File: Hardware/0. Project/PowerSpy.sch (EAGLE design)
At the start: 91 parts, among them IC1 CP2102N-A01-GQFN28, IC3 LM324D, P1 Mini-Fit 4T, T1 SS8050, T2 SS8050, U1 NCP1117ST33T3G, U2 HLK-PM01, U3 ADS1115IDGST, U4 ESP32-WROOM-32D, X1 4T PJ-321, X2 4T PJ-321, X3 USB Micro B

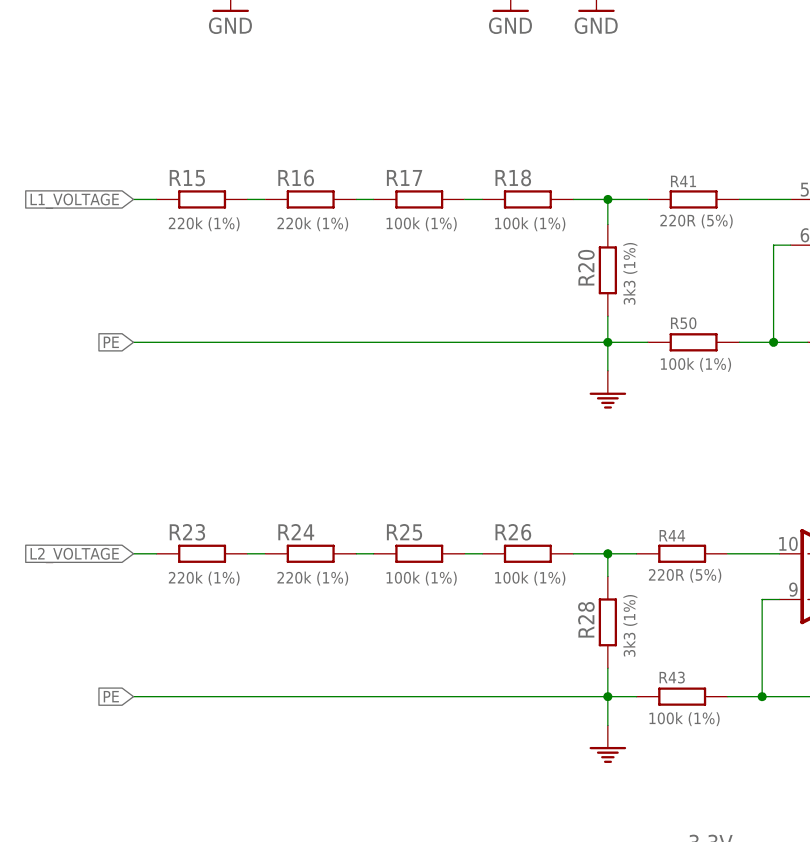
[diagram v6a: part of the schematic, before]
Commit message: Calcs and values updated for the new AFE approach
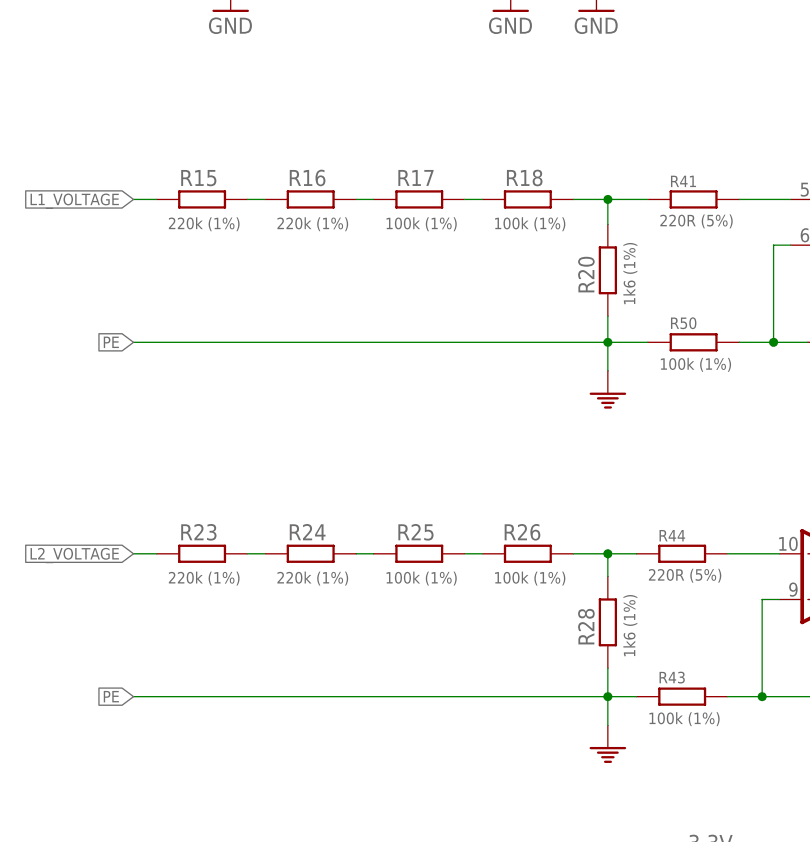
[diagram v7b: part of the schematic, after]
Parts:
- R20, R28: value 3k3 (1%) -> 1k6 (1%)
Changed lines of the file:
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@@
 <setting verticaltext="up"/>
 </settings>
-<grid distance="0.025" unitdist="inch" unit="inch" style="lines" multiple="1" display="no" altdistance="0.01" altunitdist="inch" altunit="inch"/>
+<grid distance="0.1" unitdist="inch" unit="inch" style="lines" multiple="1" display="no" altdistance="0.01" altunitdist="inch" altunit="inch"/>
 <layers>
 <layer number="1" name="Top" color="4" fill="1" visible="no" active="no"/>
@@
 <part name="R16" library="rcl" library_urn="urn:adsk.eagle:library:334" deviceset="R-EU_" device="R0603" package3d_urn="urn:adsk.eagle:package:23555/3" value="220k (1%)"/>
 <part name="R15" library="rcl" library_urn="urn:adsk.eagle:library:334" deviceset="R-EU_" device="R0603" package3d_urn="urn:adsk.eagle:package:23555/3" value="220k (1%)"/>
-<part name="R20" library="rcl" library_urn="urn:adsk.eagle:library:334" deviceset="R-EU_" device="R0603" package3d_urn="urn:adsk.eagle:package:23555/3" value="3k3 (1%)"/>
+<part name="R20" library="rcl" library_urn="urn:adsk.eagle:library:334" deviceset="R-EU_" device="R0603" package3d_urn="urn:adsk.eagle:package:23555/3" value="1k6 (1%)"/>
 <part name="R19" library="rcl" library_urn="urn:adsk.eagle:library:334" deviceset="R-EU_" device="R0603" package3d_urn="urn:adsk.eagle:package:23555/3" value="47R (5%)"/>
 <part name="C7" library="rcl" library_urn="urn:adsk.eagle:library:334" deviceset="C-EU" device="C0603K" package3d_urn="urn:adsk.eagle:package:23680/2" value="10nF/50V (10%)"/>
@@
 <part name="R24" library="rcl" library_urn="urn:adsk.eagle:library:334" deviceset="R-EU_" device="R0603" package3d_urn="urn:adsk.eagle:package:23555/3" value="220k (1%)"/>
 <part name="R23" library="rcl" library_urn="urn:adsk.eagle:library:334" deviceset="R-EU_" device="R0603" package3d_urn="urn:adsk.eagle:package:23555/3" value="220k (1%)"/>
-<part name="R28" library="rcl" library_urn="urn:adsk.eagle:library:334" deviceset="R-EU_" device="R0603" package3d_urn="urn:adsk.eagle:package:23555/3" value="3k3 (1%)"/>
+<part name="R28" library="rcl" library_urn="urn:adsk.eagle:library:334" deviceset="R-EU_" device="R0603" package3d_urn="urn:adsk.eagle:package:23555/3" value="1k6 (1%)"/>
 <part name="R39" library="rcl" library_urn="urn:adsk.eagle:library:334" deviceset="R-EU_" device="R0603" package3d_urn="urn:adsk.eagle:package:23555/3" value="1M (5%)"/>
 <part name="GND32" library="supply1" library_urn="urn:adsk.eagle:library:371" deviceset="GND" device=""/>
@@
 </instance>
 <instance part="R18" gate="G$1" x="76.2" y="132.08" smashed="yes">
-<attribute name="NAME" x="72.39" y="133.5786" size="1.778" layer="95"/>
+<attribute name="NAME" x="73.66" y="133.5786" size="1.778" layer="95"/>
 <attribute name="VALUE" x="72.39" y="128.778" size="1.27" layer="96"/>
 </instance>
 <instance part="R17" gate="G$1" x="64.135" y="132.08" smashed="yes">
-<attribute name="NAME" x="60.325" y="133.5786" size="1.778" layer="95"/>
+<attribute name="NAME" x="61.595" y="133.5786" size="1.778" layer="95"/>
 <attribute name="VALUE" x="60.325" y="128.778" size="1.27" layer="96"/>
 </instance>
 <instance part="R16" gate="G$1" x="52.07" y="132.08" smashed="yes">
-<attribute name="NAME" x="48.26" y="133.5786" size="1.778" layer="95"/>
+<attribute name="NAME" x="49.53" y="133.5786" size="1.778" layer="95"/>
 <attribute name="VALUE" x="48.26" y="128.778" size="1.27" layer="96"/>
 </instance>
 <instance part="R15" gate="G$1" x="40.005" y="132.08" smashed="yes">
-<attribute name="NAME" x="36.195" y="133.5786" size="1.778" layer="95"/>
+<attribute name="NAME" x="37.465" y="133.5786" size="1.778" layer="95"/>
 <attribute name="VALUE" x="36.195" y="128.778" size="1.27" layer="96"/>
 </instance>
 <instance part="R20" gate="G$1" x="85.09" y="124.206" smashed="yes" rot="R270">
-<attribute name="NAME" x="83.5914" y="122.301" size="1.778" layer="95" rot="R90"/>
+<attribute name="NAME" x="83.5914" y="121.539" size="1.778" layer="95" rot="R90"/>
 <attribute name="VALUE" x="86.868" y="127.381" size="1.27" layer="96" rot="R270"/>
 </instance>
@@
 </instance>
 <instance part="R26" gate="G$1" x="76.2" y="92.71" smashed="yes">
-<attribute name="NAME" x="72.39" y="94.2086" size="1.778" layer="95"/>
+<attribute name="NAME" x="73.406" y="94.2086" size="1.778" layer="95"/>
 <attribute name="VALUE" x="72.39" y="89.408" size="1.27" layer="96"/>
 </instance>
 <instance part="R25" gate="G$1" x="64.135" y="92.71" smashed="yes">
-<attribute name="NAME" x="60.325" y="94.2086" size="1.778" layer="95"/>
+<attribute name="NAME" x="61.595" y="94.2086" size="1.778" layer="95"/>
 <attribute name="VALUE" x="60.325" y="89.408" size="1.27" layer="96"/>
 </instance>
 <instance part="R24" gate="G$1" x="52.07" y="92.71" smashed="yes">
-<attribute name="NAME" x="48.26" y="94.2086" size="1.778" layer="95"/>
+<attribute name="NAME" x="49.53" y="94.2086" size="1.778" layer="95"/>
 <attribute name="VALUE" x="48.26" y="89.408" size="1.27" layer="96"/>
 </instance>
 <instance part="R23" gate="G$1" x="40.005" y="92.71" smashed="yes">
-<attribute name="NAME" x="36.195" y="94.2086" size="1.778" layer="95"/>
+<attribute name="NAME" x="37.465" y="94.2086" size="1.778" layer="95"/>
 <attribute name="VALUE" x="36.195" y="89.408" size="1.27" layer="96"/>
 </instance>
 <instance part="R28" gate="G$1" x="85.09" y="85.09" smashed="yes" rot="R270">
-<attribute name="NAME" x="83.5914" y="83.185" size="1.778" layer="95" rot="R90"/>
+<attribute name="NAME" x="83.5914" y="82.423" size="1.778" layer="95" rot="R90"/>
 <attribute name="VALUE" x="86.868" y="88.265" size="1.27" layer="96" rot="R270"/>
 </instance>

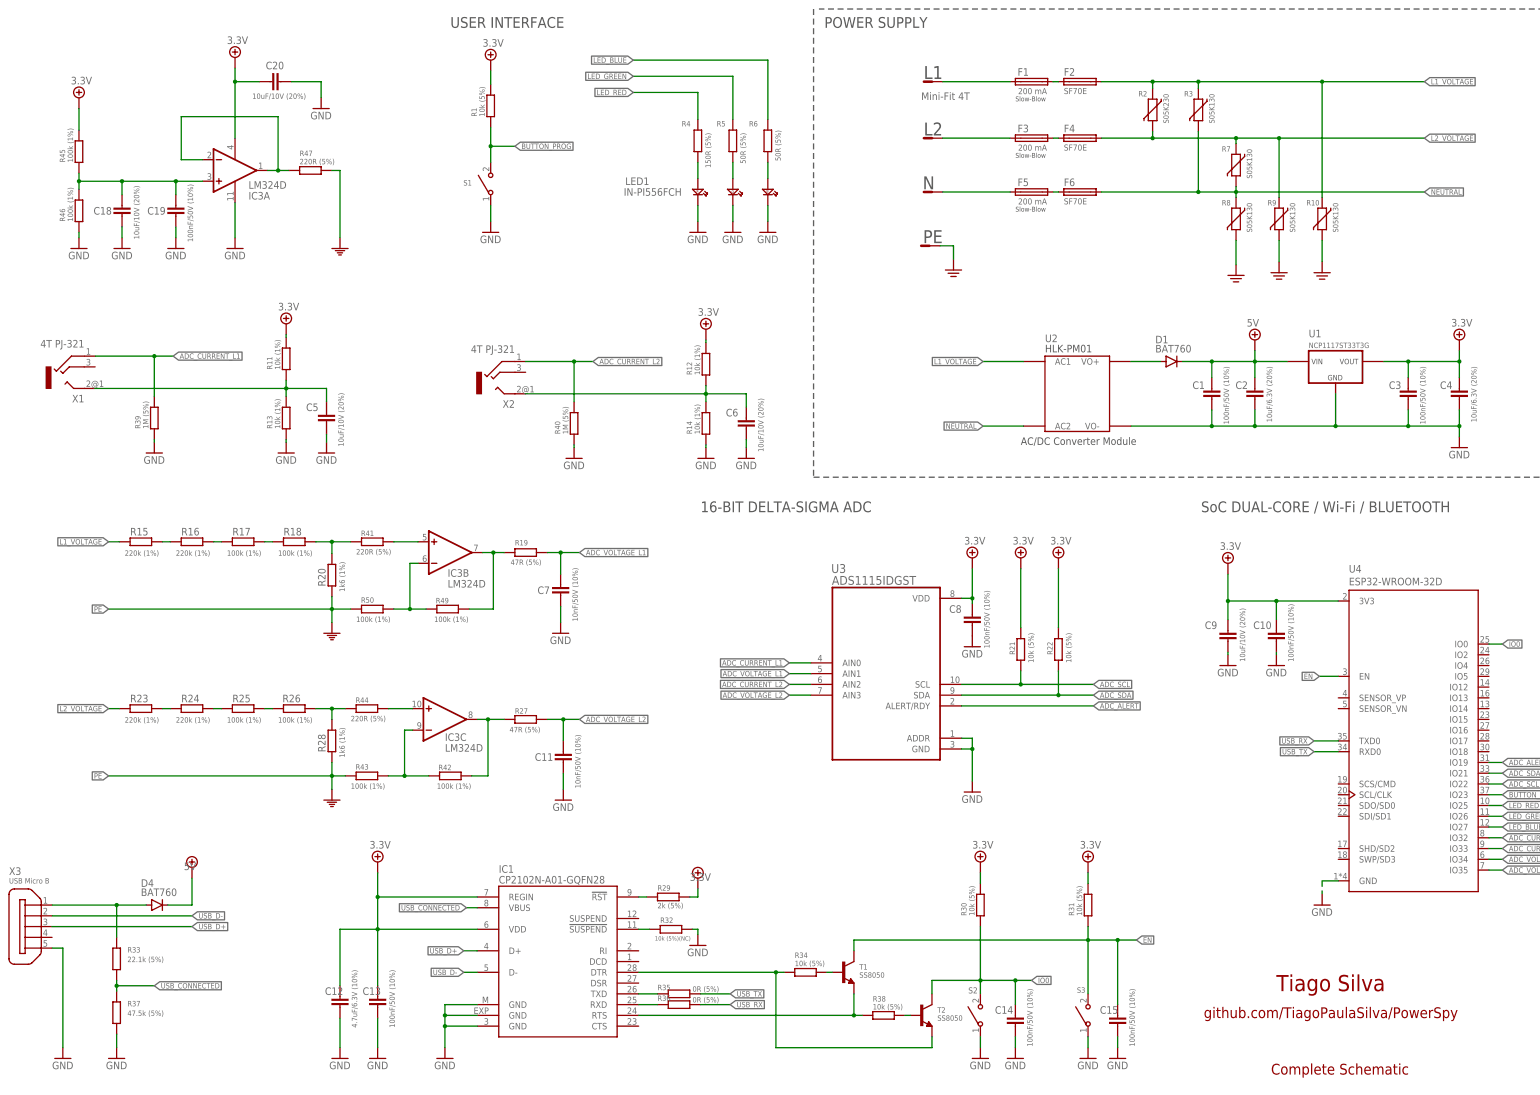
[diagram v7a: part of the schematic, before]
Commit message: Schematic parts renumbered
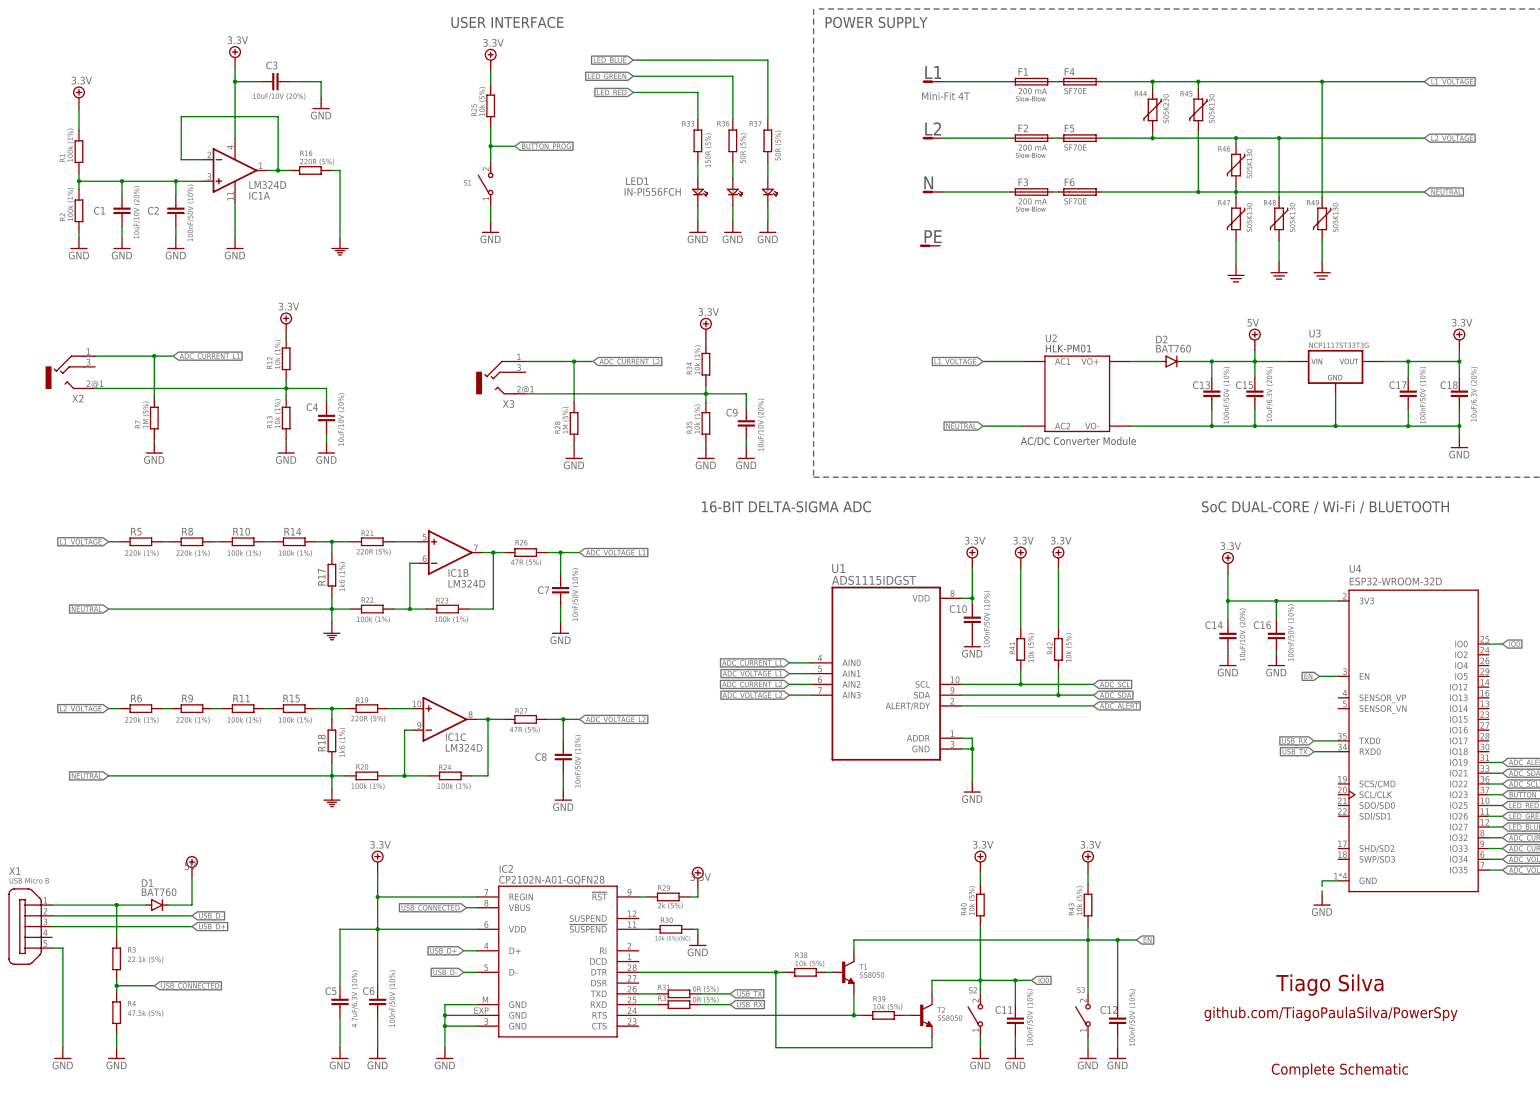
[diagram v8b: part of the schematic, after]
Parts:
- removed C19: 100nF/50V (10%), rcl:C-EUC0603K
- removed C20: 10uF/10V (20%), rcl:C-EUC0603K
- removed D4: BAT760, diode:DIODE-SOD323-W
- removed IC3: LM324D, linear:LM324D
- removed R50: 100k (1%), rcl:R-EU_R0603
- added C16, C17: 100nF/50V (10%), rcl:C-EUC0603K
- added D2: BAT760, diode:DIODE-SOD323-W
- added IC2: CP2102N-A01-GQFN28, silabs:CP2102
- added R48: S05K130, varistor:VARISTORS05K11
- C1, C14, C3: value 100nF/50V (10%) -> 10uF/10V (20%)
- C11: value 10nF/50V (10%) -> 100nF/50V (10%)
- C12: value 4.7uF/6.3V (10%) -> 100nF/50V (10%)
- C15: value 100nF/50V (10%) -> 10uF/6.3V (20%)
- C18: value 10uF/10V (20%) -> 10uF/6.3V (20%)
- C2: value 10uF/6.3V (20%) -> 100nF/50V (10%)
- C4: value 10uF/6.3V (20%) -> 10uF/10V (20%)
- C5: value 10uF/10V (20%) -> 4.7uF/6.3V (10%)
- C6: value 10uF/10V (20%) -> 100nF/50V (10%)
- C8: value 100nF/50V (10%) -> 10nF/50V (10%)
- F2: value SF70E -> 200 mA; device fuse:LITTLEFUSE -> fuse:QPL
- F5: value 200 mA -> SF70E; device fuse:QPL -> fuse:LITTLEFUSE
- IC1: value CP2102N-A01-GQFN28 -> LM324D; device silabs:CP2102 -> linear:LM324D
- R1, R22: value 10k (5%) -> 100k (1%)
- R10: value S05K130 -> 100k (1%); device varistor:VARISTORS05K11 -> rcl:R-EU_R0603
- R11, R14: value 10k (1%) -> 100k (1%)
- R15, R23, R24: value 220k (1%) -> 100k (1%)
- R16: value 220k (1%) -> 220R (5%)
- R17, R18: value 100k (1%) -> 1k6 (1%)
- R19: value 47R (5%) -> 220R (5%)
- R2: value S05K230 -> 100k (1%); device varistor:VARISTORS05K11 -> rcl:R-EU_R0603
- R20: value 1k6 (1%) -> 100k (1%)
- R21: value 10k (5%) -> 220R (5%)
- R25, R42, R43: value 100k (1%) -> 10k (5%)
- R26: value 100k (1%) -> 47R (5%)
- R28: value 1k6 (1%) -> 1M (5%)
- R3: value S05K130 -> 22.1k (5%); device varistor:VARISTORS05K11 -> rcl:R-EU_R0603
- R30: value 10k (5%) -> 10k (5%)(NC)
- R31: value 10k (5%) -> 0R (5%)
- R32: value 10k (5%)(NC) -> 0R (5%)
- R33: value 22.1k (5%) -> 150R (5%)
- R34: value 10k (5%) -> 10k (1%)
- R35: value 0R (5%) -> 10k (1%)
- R36: value 0R (5%) -> 50R (5%)
- R37: value 47.5k (5%) -> 50R (5%)
- R39, R40: value 1M (5%) -> 10k (5%)
- R4: value 150R (5%) -> 47.5k (5%)
- R41: value 220R (5%) -> 10k (5%)
- R44: value 220R (5%) -> S05K230; device rcl:R-EU_R0603 -> varistor:VARISTORS05K11
- R45, R46, R49: value 100k (1%) -> S05K130; device rcl:R-EU_R0603 -> varistor:VARISTORS05K11
- R47: value 220R (5%) -> S05K130; device rcl:R-EU_R0603 -> varistor:VARISTORS05K11
- R5, R6: value 50R (5%) -> 220k (1%)
- R7: value S05K130 -> 1M (5%); device varistor:VARISTORS05K11 -> rcl:R-EU_R0603
- R8, R9: value S05K130 -> 220k (1%); device varistor:VARISTORS05K11 -> rcl:R-EU_R0603
- U1: value NCP1117ST33T3G -> ADS1115IDGST; device REG1117:REG1117 -> ADS1115IDGST:ADS1115IDGST
- U3: value ADS1115IDGST -> NCP1117ST33T3G; device ADS1115IDGST:ADS1115IDGST -> REG1117:REG1117
- X1: value 4T PJ-321 -> USB Micro B; device con-lumberg:1503_07 -> Micro USB Connector:ZX62D-B-5PA8
- X2: value 4T PJ-321 -> 1503_07
- X3: value USB Micro B -> 1503_07; device Micro USB Connector:ZX62D-B-5PA8 -> con-lumberg:1503_07
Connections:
- removed net PE: P1-4.P, R10.2, R20.2, R28.2, R43.2, R47.1, R50.2, R8.2, R9.2
- net +4.1V: now also C3.1, IC1P.V+; no longer C20.1, IC3P.V+
- net 3.3V: now also C14.1, C16.1, C17.1, C18.1, C5.1, C6.1, IC2.REGIN, IC2.VDD, R25.1, R34.1, R40.1, R41.1, R42.1, R43.1, U1.VDD, U3.VOUT; no longer C12.1, C13.1, C3.1, C4.1, C8.1, C9.1, IC1.REGIN, IC1.VDD, R11.1, R21.1, R22.1, R30.1, R31.1, R45.1, U1.VOUT, U3.VDD
- net 5V: now also C13.1, C15.1, D2.C, U3.VIN; no longer C1.1, C2.1, D4.C, U1.VIN
- net ADC_ALERT: now also U1.ALERT/RDY; no longer U3.ALERT/RDY
- net ADC_CURRENT_L1: now also R7.1, U1.AIN0, X2.1; no longer R39.1, U3.AIN0, X1.1
- net ADC_CURRENT_L2: now also R28.1, U1.AIN2, X3.1; no longer R40.1, U3.AIN2, X2.1
- net ADC_SCL: now also R41.2, U1.SCL; no longer R21.2, U3.SCL
- net ADC_SDA: now also R42.2, U1.SDA; no longer R22.2, U3.SDA
- net ADC_VOLTAGE_L1: now also R26.1, U1.AIN1; no longer R19.1, U3.AIN1
- net ADC_VOLTAGE_L2: now also C8.1, U1.AIN3; no longer C11.1, U3.AIN3
- net BUTTON_PROG: now also R25.2; no longer R1.2
- net DTR: now also IC2.DTR, R38.2; no longer IC1.DTR, R34.2
- net EN: now also C12.1, R43.2; no longer C15.1, R31.2
- net GND: now also C16.2, C17.2, IC1P.V-, IC2.GND, IC2.GND@EXP, IC2.GND@M, R2.2, R28.2, R30.1, R35.2, R4.1, R7.2, U1.ADDR, X1G$1.5; no longer C19.2, C20.2, IC1.GND, IC1.GND@EXP, IC1.GND@M, IC3P.V-, R14.2, R32.1, R37.1, R39.2, R40.2, R46.2, U3.ADDR, X3G$1.5
- net IO0: now also C11.1, R40.2; no longer C14.1, R30.2
- net L1_VOLTAGE: now also F4.2, R44.1, R45.1, R49.1, R5.1; no longer F2.2, R10.1, R15.1, R2.1, R3.1
- net L2_VOLTAGE: now also F5.2, R44.2, R46.1, R48.1, R6.1; no longer F4.2, R2.2, R23.1, R7.1, R9.1
- net LED_BLUE: now also R37.1; no longer R6.1
- net LED_GREEN: now also R36.1; no longer R5.1
- net LED_RED: now also R33.1; no longer R4.1
- net N$1: now also IC2.!SUSPEND, R30.2; no longer IC1.!SUSPEND, R32.2
- net N$10: now also IC2.RXD, R32.2; no longer IC1.RXD, R36.2
- net N$11: now also C4.1, R12.2, X2.2; no longer C5.1, R11.2, X1.2
- net N$12: now also R10.1, R8.2; no longer R16.2, R17.1
- net N$13: now also IC1A.-IN, IC1A.OUT, R16.2; no longer IC3A.-IN, IC3A.OUT, R47.2
- net N$14: now also C1.1, C2.1, IC1A.+IN, R1.2, R2.1; no longer C18.1, C19.1, IC3A.+IN, R45.2, R46.1
- net N$15: now also IC1B.OUT, R23.1, R26.2; no longer IC3B.OUT, R19.2, R49.1
- net N$16: now also R15.2, R18.1, R19.2; no longer R26.2, R28.1, R44.2
- net N$17: now also F3.1; no longer F5.1
- net N$18: now also R10.2, R14.1; no longer R17.2, R18.1
- net N$19: now also R5.2, R8.1; no longer R15.2, R16.1
- net N$2: now also IC2.!RST; no longer IC1.!RST
- net N$20: now also IC1C.OUT, R24.1; no longer IC3C.OUT, R42.1
- net N$21: now also R36.2; no longer R5.2
- net N$22: now also C9.1, R34.2, R35.1, X3.2; no longer C6.1, R12.2, R14.1, X2.2
- net N$24: now also F2.2; no longer F3.2
- net N$25: now also F3.2; no longer F5.2
- net N$26: now also R37.2; no longer R6.2
- net N$27: now also R11.1, R9.2; no longer R24.2, R25.1
- net N$28: now also R11.2, R15.1; no longer R25.2, R26.1
- net N$29: now also R6.2, R9.1; no longer R23.2, R24.1
- net N$3: now also R33.2; no longer R4.2
- net N$30: now also IC1B.-IN, R22.1, R23.2; no longer IC3B.-IN, R49.2, R50.1
- net N$31: now also R14.2, R17.1, R21.2; no longer R18.2, R20.1, R41.2
- net N$32: now also IC1B.+IN, R21.1; no longer IC3B.+IN, R41.1
- net N$33: now also IC1C.-IN, R20.1, R24.2; no longer IC3C.-IN, R42.2, R43.1
- net N$34: now also IC1C.+IN, R19.1; no longer IC3C.+IN, R44.1
- net N$4: now also F4.1; no longer F2.1
- net N$5: now also R39.1; no longer R38.1
- net N$6: now also D2.A; no longer D1.A
- net N$7: now also R38.1; no longer R34.1
- net N$8: now also IC2.TXD, R31.2; no longer IC1.TXD, R35.2
- net N$9: now also F2.1, F5.1; no longer F3.1, F4.1
- net NEUTRAL: now also R16.1, R17.2, R18.2, R20.2, R22.2, R45.2, R46.2, R47.1, R47.2, R48.2, R49.2; no longer R3.2, R7.2, R8.1
- net RTS: now also IC2.RTS, R39.2; no longer IC1.RTS, R38.2
- net USB_CONNECTED: now also IC2.VBUS, R3.1, R4.2; no longer IC1.VBUS, R33.1, R37.2
- net USB_D+: now also IC2.D+, X1G$1.3; no longer IC1.D+, X3G$1.3
- net USB_D-: now also IC2.D-, X1G$1.2; no longer IC1.D-, X3G$1.2
- net USB_RX: now also R32.1; no longer R36.1
- net USB_TX: now also R31.1; no longer R35.1
- net VUSB: now also D1.A, R3.2, X1G$1.1; no longer D4.A, R33.2, X3G$1.1
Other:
- moved on the sheet: C1, C10, C11, C12, C13, C14, C15, C18, C2, C3, C4, C5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
